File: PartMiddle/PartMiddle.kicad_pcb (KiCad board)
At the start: 2 copper layers, 79.5 x 70 mm, 14 parts, among them J1 MiddleHalf, J2 Middle, SW1 SW_Push, SW2 SW_Push, SW3 SW_Push, SW4 SW_Push, SW5 SW_Push, SW6 SW_Push

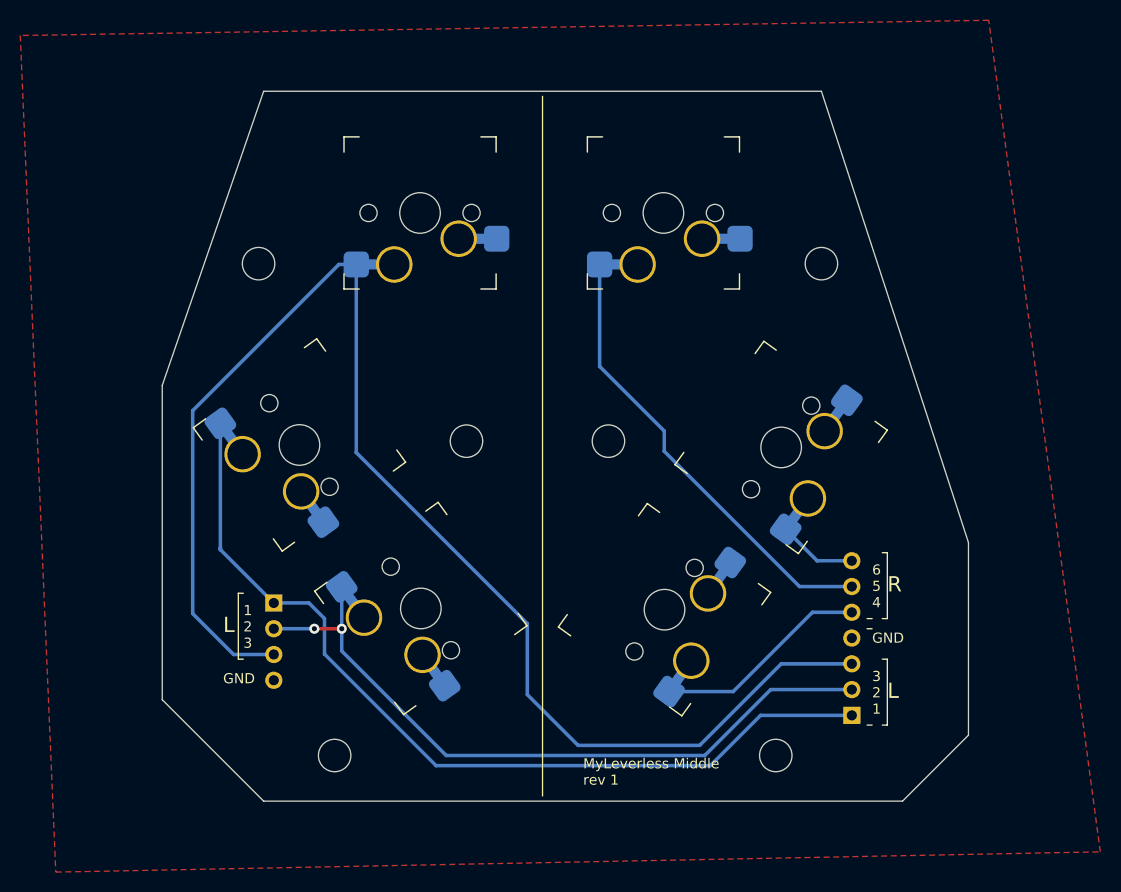
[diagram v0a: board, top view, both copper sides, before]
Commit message: Realign middle part pings to the right part.
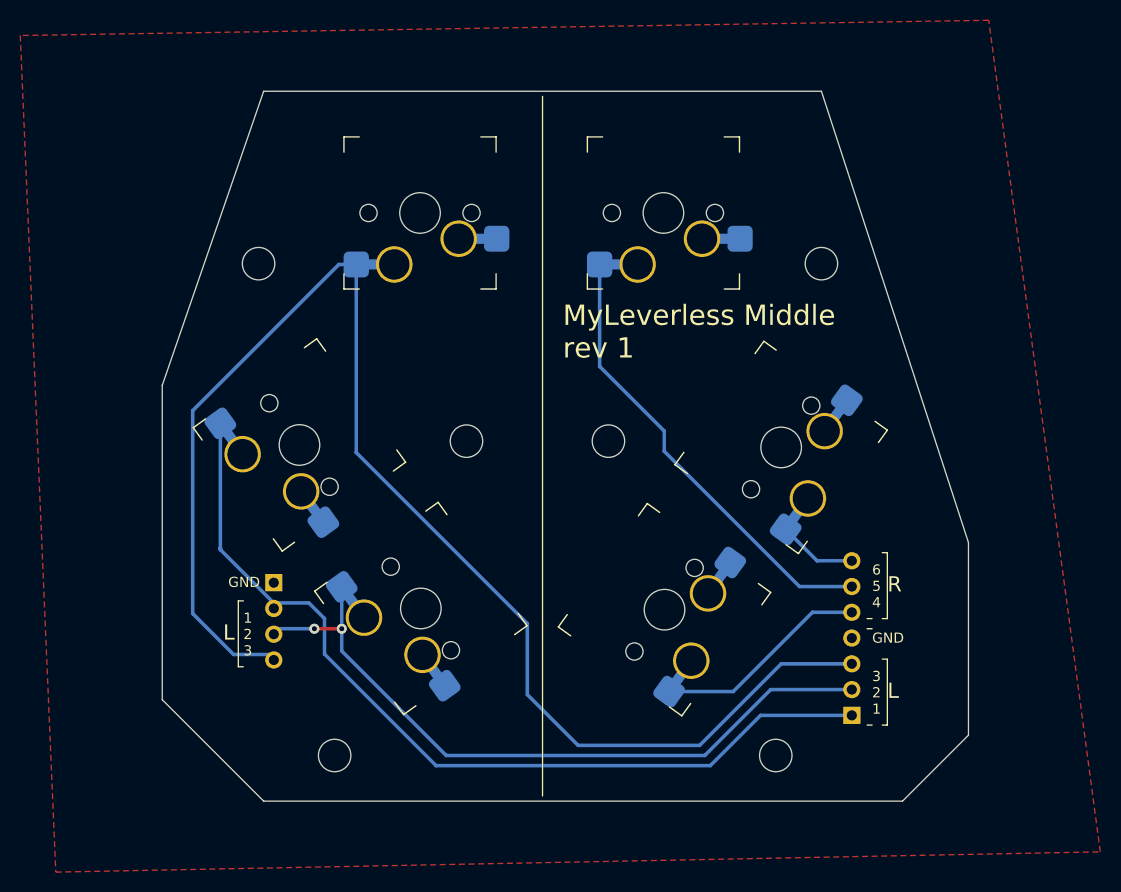
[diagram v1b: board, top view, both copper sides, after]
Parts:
- moved J1 2.00 mm to (92.0, 151.5)
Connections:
- J1 pad 1: M_SW1 -> GND
- J1 pad 2: M_SW2 -> M_SW1
- J1 pad 3: M_SW3 -> M_SW2
- J1 pad 4: GND -> M_SW3
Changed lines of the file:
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@@
 	(footprint "Connector_PinHeader_2.54mm:PinHeader_1x04_P2.54mm_Horizontal"
 		(layer "B.Cu")
-		(at 92 153.46 180)
+		(at 92 151.46 180)
 		(descr "Through hole angled pin header, 1x04, 2.54mm pitch, 6mm pin length, single row")
 		(tags "Through hole angled pin header THT 1x04 2.54mm single row")
@@
 			(layers "*.Cu" "*.Mask")
 			(remove_unused_layers no)
-			(net 2 "M_SW1")
+			(net 6 "GND")
 			(pinfunction "Pin_1")
 			(pintype "passive")
@@
 			(layers "*.Cu" "*.Mask")
 			(remove_unused_layers no)
-			(net 3 "M_SW2")
+			(net 2 "M_SW1")
 			(pinfunction "Pin_2")
 			(pintype "passive")
@@
 			(layers "*.Cu" "*.Mask")
 			(remove_unused_layers no)
-			(net 1 "M_SW3")
+			(net 3 "M_SW2")
 			(pinfunction "Pin_3")
 			(pintype "passive")
@@
 			(layers "*.Cu" "*.Mask")
 			(remove_unused_layers no)
-			(net 6 "GND")
+			(net 1 "M_SW3")
 			(pinfunction "Pin_4")
 			(pintype "passive")
@@
 	)
 	(gr_line
-		(start 88.5 152.5)
-		(end 89 152.5)
+		(start 88.5 153.25)
+		(end 89 153.25)
 		(stroke
 			(width 0.1)
@@
 	)
 	(gr_line
-		(start 88.5 152.5)
-		(end 88.5 159)
+		(start 88.5 153.25)
+		(end 88.5 159.75)
 		(stroke
 			(width 0.1)
@@
 	)
 	(gr_line
-		(start 89 159)
-		(end 88.5 159)
+		(start 89 159.75)
+		(end 88.5 159.75)
 		(stroke
 			(width 0.1)
@@
 	)
 	(gr_text "GND"
-		(at 87 161.5 0)
+		(at 87.5 152 0)
 		(layer "F.SilkS")
 		(effects
@@
 	)
 	(gr_text "1\n2\n3"
-		(at 89 158 0)
+		(at 89 158.75 0)
 		(layer "F.SilkS")
 		(effects
@@
 	)
 	(gr_text "L"
-		(at 87 156.5 0)
+		(at 87 157.25 0)
 		(layer "F.SilkS")
 		(effects
@@
 	)
 	(gr_text "MyLeverless Middle\nrev 1"
-		(at 122.5 171.5 0)
+		(at 120.5 129.5 0)
 		(layer "F.SilkS")
 		(effects
 			(font
-				(size 1 1)
-				(thickness 0.1)
+				(size 2 2)
+				(thickness 0.2)
 			)
 			(justify left bottom)

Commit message: Fix some rule checks.
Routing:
- net M_SW1: track 87.9 -> 89.6 mm
